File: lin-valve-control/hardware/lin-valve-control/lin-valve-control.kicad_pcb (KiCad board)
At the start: 2 copper layers, 34 parts, among them J1 Conn_02x03_Odd_Even, J2 Screw_Terminal_01x03, J3 Screw_Terminal_01x03, U1 SN74AHCT1G86DCKT, U2 ATA6614Q-PLQW-1, U3 SN74LVC2G08DCUT, U4 CPC1002N, U5 CPC1002N, U6 LMV358

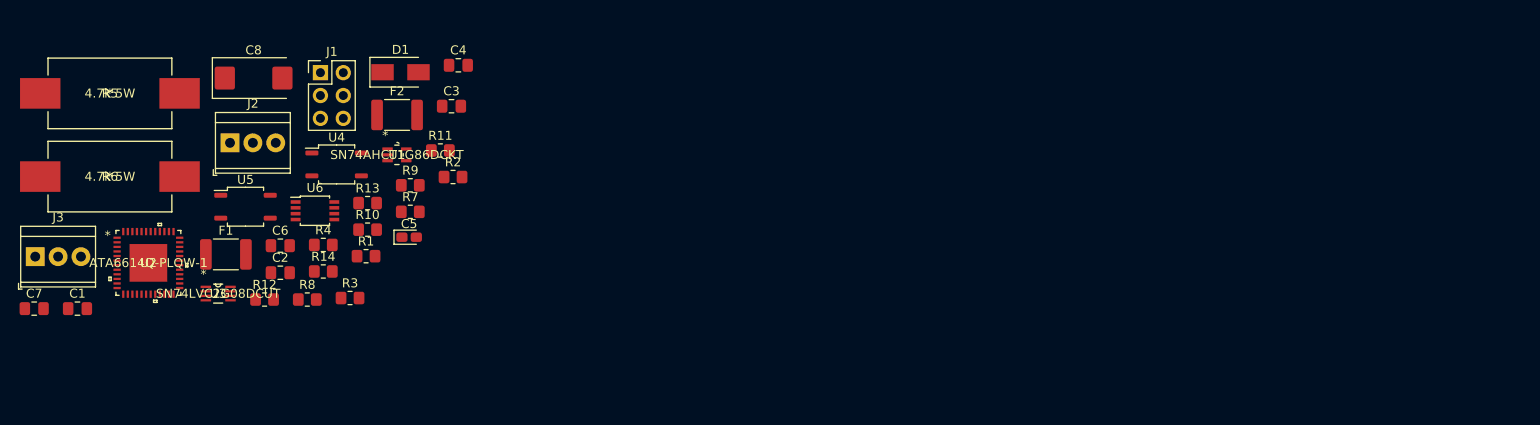
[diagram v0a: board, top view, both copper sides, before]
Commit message: Redo the valve controller using an Arduino Nano
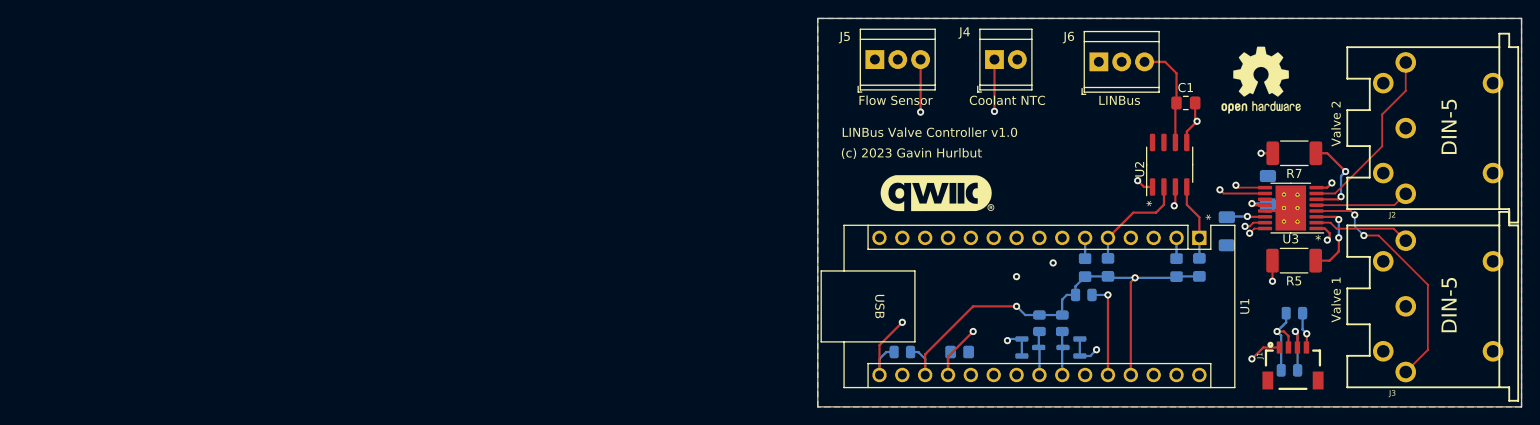
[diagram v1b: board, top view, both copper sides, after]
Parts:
- removed C4, C7: 100nF, Capacitor_SMD:C_0805_2012Metric_Pad1.18x1.45mm_HandSolder
- removed C5: 10uF 10V Ta, Capacitor_Tantalum_SMD:CP_EIA-1608-10_AVX-L_Pad1.25x1.05mm_HandSolder
- removed C6: 220pF, Capacitor_SMD:C_0805_2012Metric_Pad1.18x1.45mm_HandSolder
- removed C8: 22uF 25V Ta, Capacitor_Tantalum_SMD:CP_EIA-7343-31_Kemet-D_Pad2.25x2.55mm_HandSolder
- removed D1: B160-E3, Diode_SMD:D_SMA
- removed F1, F2: 500mA Polyfuse, Fuse:Fuse_1812_4532Metric_Pad1.30x3.40mm_HandSolder
- removed R14: 10k, Resistor_SMD:R_0805_2012Metric_Pad1.20x1.40mm_HandSolder
- removed U4, U5: CPC1002N, Package_SO:SOP-4_3.8x4.1mm_P2.54mm
- removed U6: LMV358, Package_SO:TSSOP-8_3x3mm_P0.65mm
- added G***: LOGO, Beirdo:qwiic-logo, F.Cu at (165.6, 77.7)
- added J3: DIN-5_180degree, SparkFun-Connectors:DIN5-RA-PTH, F.Cu at (230.3, 90.4)
- added J4: Screw_Terminal_01x02, TerminalBlock_TE-Connectivity:TerminalBlock_TE_282834-2_1x02_P2.54mm_Horizontal, F.Cu at (172.0, 63.0)
- added J5: Screw_Terminal_01x03, TerminalBlock_TE-Connectivity:TerminalBlock_TE_282834-3_1x03_P2.54mm_Horizontal, F.Cu at (158.8, 63.0)
- added Q1: 2N7002, Package_TO_SOT_SMD:SOT-23, B.Cu at (180.6, 95.0)
- added Q2: 2N7002, Package_TO_SOT_SMD:SOT-23, B.Cu at (176.0, 95.0)
- added REF**: OSHW-Logo2_9.8x8mm_SilkScreen, Symbol:OSHW-Logo2_9.8x8mm_SilkScreen, F.Cu at (201.7, 65.3)
- C1: value 100nF -> 220pF
- C2: value 100nF -> 10uF 16V; footprint Capacitor_SMD:C_0805_2012Metric_Pad1.18x1.45mm_HandSolder -> Capacitor_SMD:C_1206_3216Metric_Pad1.33x1.80mm_HandSolder; moved to B.Cu
- C3: value 100nF -> 2.2uF 6.3V; footprint Capacitor_SMD:C_0805_2012Metric_Pad1.18x1.45mm_HandSolder -> Capacitor_SMD:C_1206_3216Metric_Pad1.33x1.80mm_HandSolder; moved to B.Cu
- J1: value Conn_02x03_Odd_Even -> QWIIC Connector; footprint Connector_PinHeader_2.54mm:PinHeader_2x03_P2.54mm_Vertical -> SparkFun-Connectors:1X04_1MM_RA
- J2: value Screw_Terminal_01x03 -> DIN-5_180degree; footprint TerminalBlock_TE-Connectivity:TerminalBlock_TE_282834-3_1x03_P2.54mm_Horizontal -> SparkFun-Connectors:DIN5-RA-PTH
- R1: moved to B.Cu
- R10, R11, R12, R13, R8, R9: footprint Resistor_SMD:R_0805_2012Metric_Pad1.20x1.40mm_HandSolder -> Resistor_SMD:R_0805_2012Metric; moved to B.Cu
- R2: value 51k -> 10k; moved to B.Cu
- R3, R4: value 1k -> 10k; moved to B.Cu
- R5: value 4.7k 5W -> 2R 2W; footprint ultralibrarian:SMF54K7JT -> Resistor_SMD:R_2010_5025Metric_Pad1.40x2.65mm_HandSolder
- R6: value 4.7k 5W -> 10k; footprint ultralibrarian:SMF54K7JT -> Resistor_SMD:R_0805_2012Metric_Pad1.20x1.40mm_HandSolder; moved to B.Cu
- R7: value 10k -> 2R 2W; footprint Resistor_SMD:R_0805_2012Metric_Pad1.20x1.40mm_HandSolder -> Resistor_SMD:R_2010_5025Metric_Pad1.40x2.65mm_HandSolder
- U1: value SN74AHCT1G86DCKT -> Arduino_Nano_v3.x; footprint ultralibrarian:SN74AHCT1G86DCKT -> Module:Arduino_Nano
- U2: value ATA6614Q-PLQW-1 -> TJA1021T; footprint ultralibrarian:ATA6614Q-PLQW-1 -> Package_SO:SOIC-8_3.9x4.9mm_P1.27mm
- U3: value SN74LVC2G08DCUT -> DRV8833PWP; footprint ultralibrarian:SN74LVC2G08DCUT -> Package_SO:HTSSOP-16-1EP_4.4x5mm_P0.65mm_EP3.4x5mm_Mask2.46x2.31mm_ThermalVias
- moved J2 143.2 mm to (230.3, 70.6), turned to 90 degrees
- moved R5 132.9 mm to (205.3, 85.3), turned to 180 degrees
- moved C1 125.3 mm to (193.3, 67.8)
- moved J6 120.2 mm to (183.6, 63.2)
- moved U3 119.6 mm to (205.0, 79.5), turned to 180 degrees
- moved R12 114.2 mm to (204.8, 97.5)
- moved U2 114.1 mm to (191.5, 74.7), turned to 90 degrees
- moved J1 112.3 mm to (205.2, 95.0)
- moved C2 110.2 mm to (202.4, 77.5), turned to 90 degrees
- moved R6 108.9 mm to (182.1, 86.1), turned to 90 degrees
- moved R13 103.8 mm to (205.4, 91.2)
- moved R7 98.5 mm to (205.4, 73.4), turned to 180 degrees
- moved R1 90.1 mm to (192.3, 86.1), turned to 90 degrees
- moved U1 89.7 mm to (194.8, 82.8), turned to -90 degrees
- moved C3 87.3 mm to (197.9, 82.1), turned to -90 degrees
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- renumbered J3 to J6
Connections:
- C1 pad 1: Net-(C1-Pad1) -> LIN
- C1 pad 2: Net-(C1-Pad2) -> GND
- C2 pad 1: +5V -> +12V
- J1 pad 1: MISO -> GND
- J1 pad 2: +5V -> +3V3
- J1 pad 3: SCK -> SDA
- J1 pad 4: MOSI -> SCL
- J2 pad 1: Net-(F1-Pad1) -> VALVE2+
- J2 pad 3: Net-(F2-Pad1) -> VALVE2-
- J6 pad 1: +5V -> +12V
- R1 pad 2: ~RESET -> RXD
- R10 pad 1: Net-(R10-Pad1) -> +5V
- R10 pad 2: OPEN -> SDA5
- R11 pad 1: Net-(R10-Pad1) -> +5V
- R11 pad 2: GND -> SCL5
- R12 pad 1: Net-(R12-Pad1) -> +3V3
- R12 pad 2: GND -> SDA
- R13 pad 1: CLOSE_SENSE -> +3V3
- R13 pad 2: Net-(R13-Pad2) -> SCL
- R2 pad 1: Net-(R2-Pad1) -> +5V
- R2 pad 2: GND -> TXD
- R3 pad 1: Net-(R3-Pad1) -> MOTOR_EN
- R3 pad 2: Net-(R3-Pad2) -> GND
- R4 pad 1: Net-(R4-Pad1) -> +5V
- R4 pad 2: Net-(R4-Pad2) -> ~{LIN_SLP}
- R5 pad 1: CLOSE -> Net-(R5-Pad1)
- R5 pad 2: CLOSE+ -> GND
- R6 pad 1: OPEN -> +5V
- R6 pad 2: OPEN+ -> ~{LIN_WAKE}
- R7 pad 1: Net-(R13-Pad2) -> Net-(R7-Pad1)
- R7 pad 2: CLOSE+ -> GND
- R8 pad 1: Net-(R12-Pad1) -> +5V
- R8 pad 2: CLOSE -> COOLANT_NTC
- R9 pad 1: Net-(R14-Pad2) -> +5V
- R9 pad 2: OPEN+ -> ~{MOTOR_FAULT}
- U1 pad 1: VALVE_OPEN -> TXD
- U1 pad 2: VALVE_CLOSE -> RXD
- U1 pad 3: GND -> unconnected-(U1-Pad3)
- U1 pad 4: Net-(U1-Pad4) -> GND
- U1 pad 5: +5V -> ~{LIN_SLP}
- U2 pad 1: SCK -> RXD
- U2 pad 2: Net-(C1-Pad1) -> ~{LIN_SLP}
- U2 pad 3: (no net) -> ~{LIN_WAKE}
- U2 pad 4: (no net) -> TXD
- U2 pad 5: Net-(C1-Pad2) -> GND
- U2 pad 6: (no net) -> LIN
- U2 pad 7: OPEN_SENSE -> +12V
- U2 pad 8: CLOSE_SENSE -> unconnected-(U2-Pad8)
- U3 pad 1: VALVE_OPEN -> MOTOR_EN
- U3 pad 2: Net-(U1-Pad4) -> VALVE1+
- U3 pad 3: Net-(R4-Pad1) -> Net-(R5-Pad1)
- U3 pad 4: GND -> VALVE1-
- U3 pad 5: VALVE_CLOSE -> VALVE2-
- U3 pad 6: Net-(U1-Pad4) -> Net-(R7-Pad1)
- U3 pad 7: Net-(R3-Pad2) -> VALVE2+
- U3 pad 8: +5V -> ~{MOTOR_FAULT}
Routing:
- net ~{MOTOR_FAULT}: track 0.00 -> 68.5 mm, vias 0 -> 2
- net VALVE2_OPEN: track 0.00 -> 60.6 mm
- net VALVE2_CLOSED: track 0.00 -> 54.9 mm
- net MOTOR_EN: track 0.00 -> 54.8 mm, vias 0 -> 2
- net +5V: track 0.00 -> 53.6 mm, vias 0 -> 2
- net +3V3: track 0.00 -> 53.4 mm, vias 0 -> 1
- net VALVE1_CLOSED: track 0.00 -> 48.5 mm, vias 0 -> 1
- net VALVE1_OPEN: track 0.00 -> 48.1 mm
- net SDA: track 0.00 -> 42.3 mm, vias 0 -> 2
- net COOLANT_NTC: track 0.00 -> 42.1 mm, vias 0 -> 2
- net VALVE_IN2-: track 0.00 -> 37.6 mm, vias 0 -> 1
- net VALVE_IN2+: track 0.00 -> 35.2 mm, vias 0 -> 1
- net SCL: track 0.00 -> 32.2 mm, vias 0 -> 2
- net VALVE_IN1+: track 0.00 -> 29.1 mm, vias 0 -> 2
- net VALVE_IN1-: track 0.00 -> 28.3 mm, vias 0 -> 1
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- added copper zone on F.Cu, net +12V
- added copper zone on B.Cu, net GND
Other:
- board outline added: 78.2 x 43.2 mm
- copper layers 2 -> 4
- net class Default removed
- board text added: "(c) 2023 Gavin Hurlbut"
- board text added: "Coolant NTC"
- board text added: "Flow Sensor"
- board text added: "LINBus"
- board text added: "LINBus Valve Controller v1.0"
- board text added: "Valve 1"
- board text added: "Valve 2"

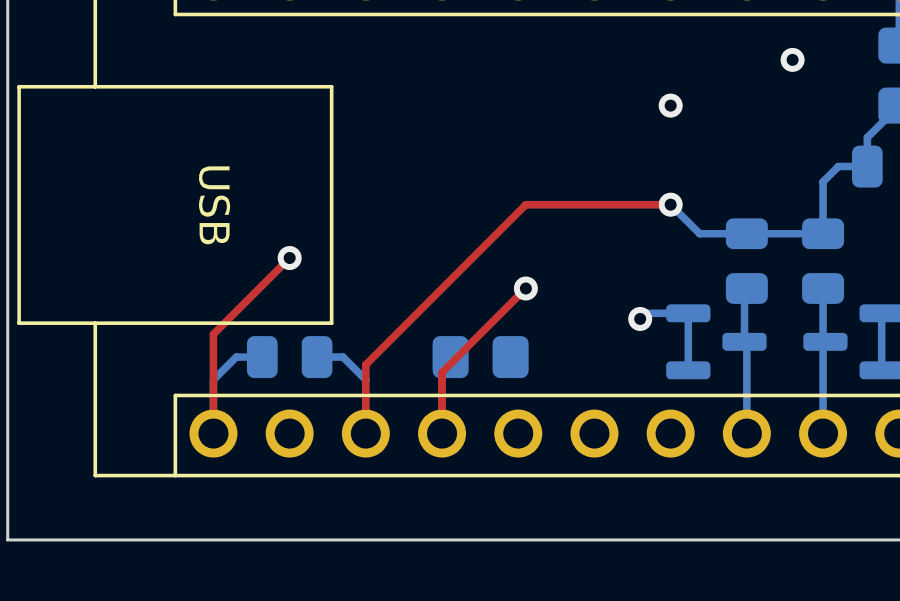
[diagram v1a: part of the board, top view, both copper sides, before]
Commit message: Move flow sensor to ICP1, run it at 5V
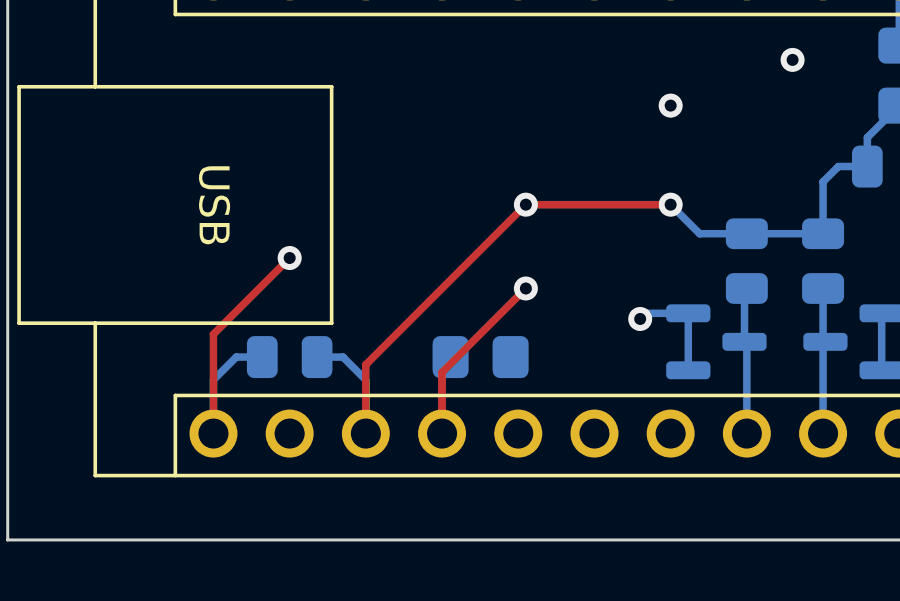
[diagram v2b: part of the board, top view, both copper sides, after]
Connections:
- J5 pad 1: +12V -> +5V
- U1 pad 11: VALVE_IN2+ -> FLOW_PULSE
- U1 pad 12: VALVE_IN2- -> VALVE_IN2+
- U1 pad 13: VALVE2_CLOSED -> VALVE_IN2-
- U1 pad 14: VALVE2_OPEN -> VALVE2_CLOSED
- U1 pad 15: FLOW_PULSE -> VALVE2_OPEN
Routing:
- net +5V: track 53.6 -> 85.6 mm, vias 2 -> 3
- net VALVE_IN2+: track 35.2 -> 37.8 mm
- net VALVE_IN2-: track 37.6 -> 40.2 mm
- net VALVE2_OPEN: track 60.6 -> 63.1 mm
- net VALVE2_CLOSED: track 54.9 -> 57.4 mm
